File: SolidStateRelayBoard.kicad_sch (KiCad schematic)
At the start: 36 parts, among them J1 CONTROL_BUS, J2 GND, J4 SolenoidValveOutput1_5, J5 SolenoidValveOutput6_10, T1 48VA Transformer 240VAC/24VAC, U1 AQH3223A, U10 AQH3223A, U2 AQH3223A, U3 AQH3223A, U4 AQH3223A, U5 AQH3223A, U6 AQH3223A, U7 AQH3223A, U8 AQH3223A, U9 AQH3223A

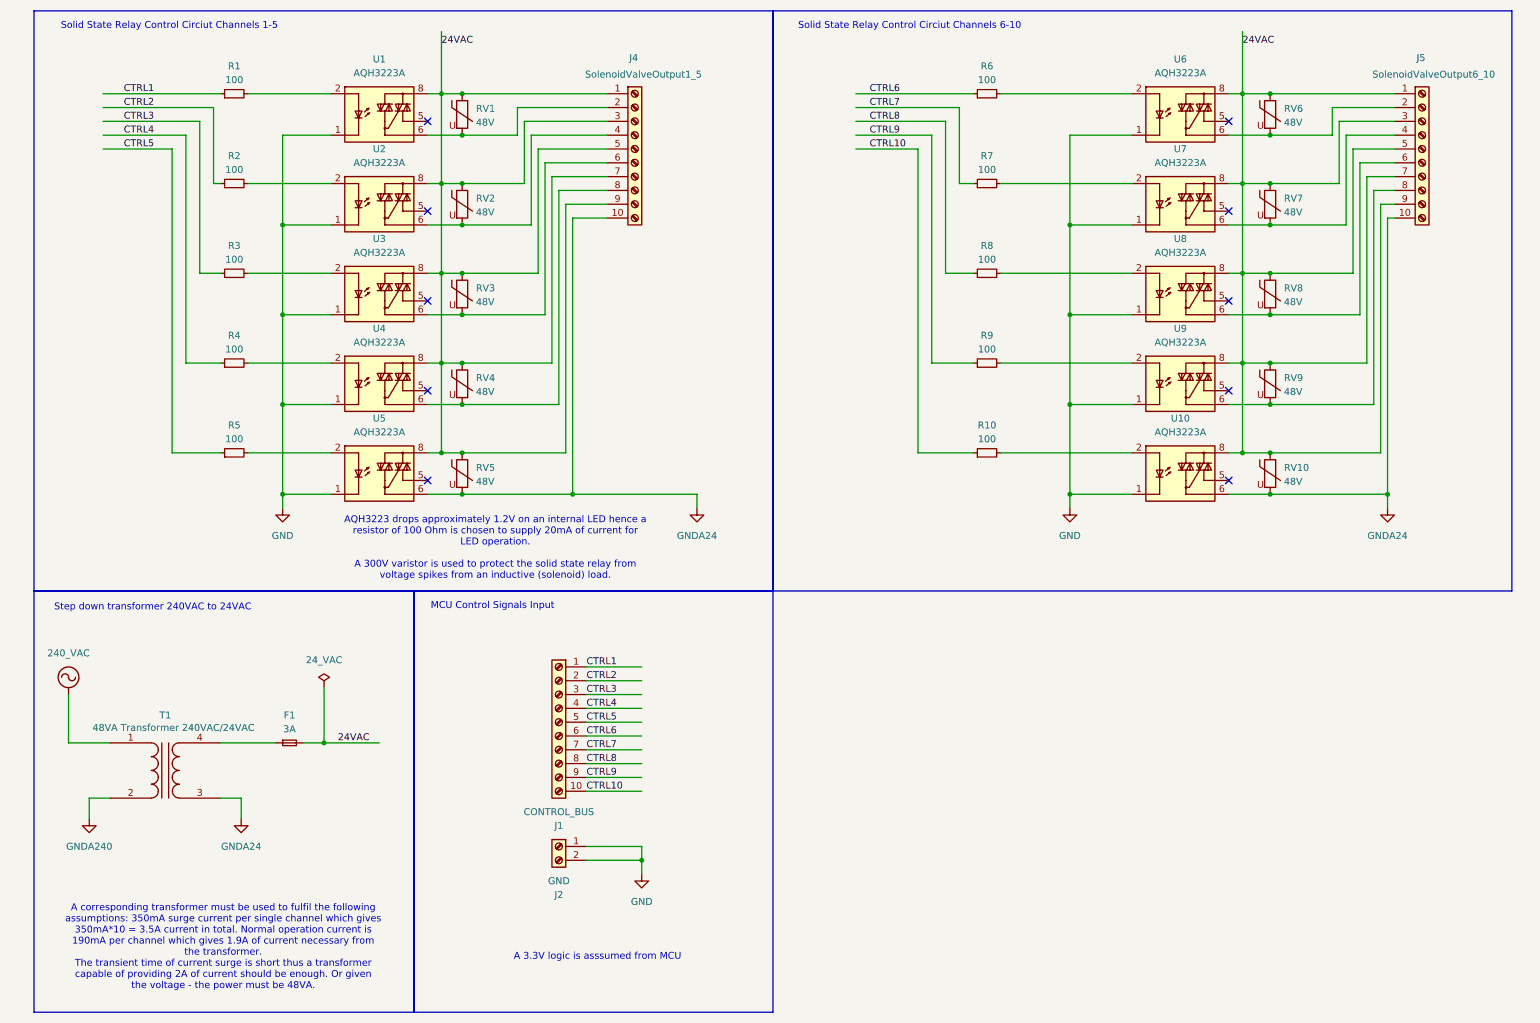
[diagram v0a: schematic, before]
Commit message: Add layout and 3D model
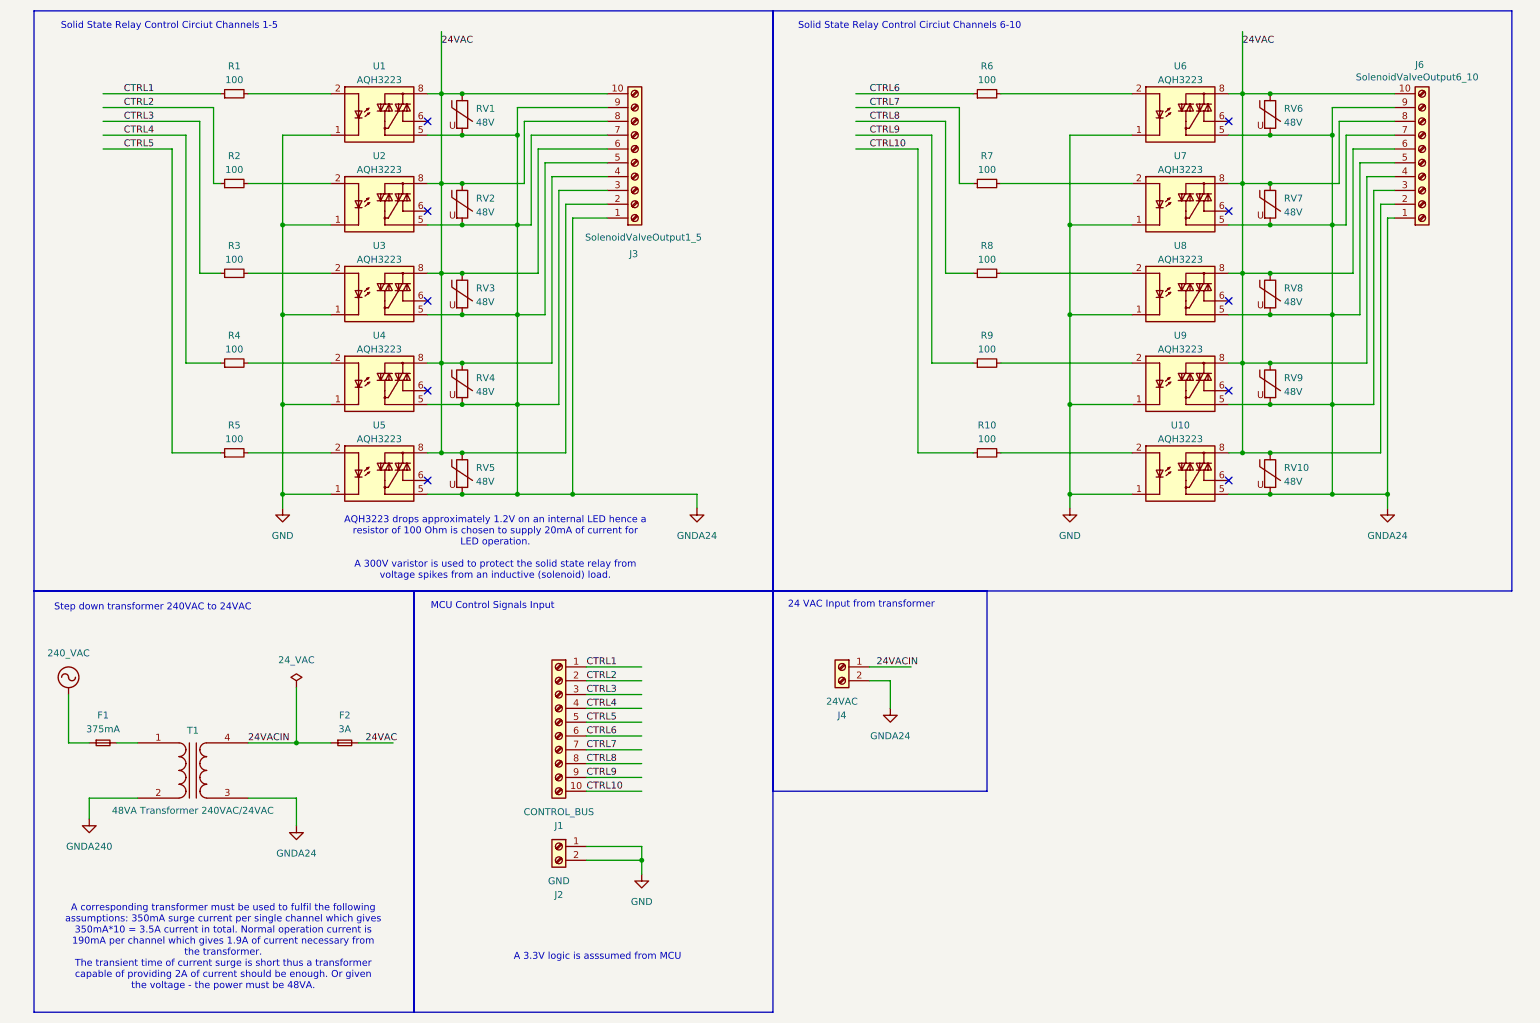
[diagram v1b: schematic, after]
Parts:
- removed J4: SolenoidValveOutput1_5, symbol Connector:Screw_Terminal_01x10
- removed J5: SolenoidValveOutput6_10, symbol Connector:Screw_Terminal_01x10
- removed U1, U10, U2, U3, U4, U5, U6, U7, U8, U9: AQH3223A, Package_SO:SSO-7-8_6.4x9.78mm_P2.54mm, symbol Relay_SolidState:AQH3223A
- added F2: 3A, Fuse:Fuseholder_Cylinder-5x20mm_Schurter_0031_8201_Horizontal_Open, symbol Device:Fuse_Small
- added J3: SolenoidValveOutput1_5, TerminalBlock_4Ucon:TerminalBlock_4Ucon_1x10_P3.50mm_Horizontal, symbol Connector:Screw_Terminal_01x10
- added J4: 24VAC, TerminalBlock_4Ucon:TerminalBlock_4Ucon_1x02_P3.50mm_Horizontal, symbol Connector:Screw_Terminal_01x02
- added J6: SolenoidValveOutput6_10, TerminalBlock_4Ucon:TerminalBlock_4Ucon_1x10_P3.50mm_Horizontal, symbol Connector:Screw_Terminal_01x10
- added U1, U10, U2, U3, U4, U5, U6, U7, U8, U9: AQH3223, Package_DIP:DIP-8-N7_W7.62mm, symbol Relay_SolidState:AQH3223
- F1: value 3A -> 375mA; footprint (none) -> Fuse:Fuseholder_Clip-5x20mm_Eaton_1A5601-01_Inline_P20.80x6.76mm_D1.70mm_Horizontal
- J1: footprint (none) -> TerminalBlock:TerminalBlock_Xinya_XY308-2.54-10P_1x10_P2.54mm_Horizontal
- J2: footprint (none) -> TerminalBlock:TerminalBlock_Xinya_XY308-2.54-2P_1x02_P2.54mm_Horizontal
- R1, R10, R2, R3, R4, R5, R6, R7, R8, R9: footprint (none) -> Resistor_SMD:R_0805_2012Metric
- RV1, RV10, RV2, RV3, RV4, RV5, RV6, RV7, RV8, RV9: footprint (none) -> Varistor:RV_Disc_D12mm_W3.9mm_P7.5mm
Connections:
- net 240_VAC: now also F1.1; no longer T1.1 (AA)
- net 24VAC: now also F2.2, J3.10 (Pin_10), J3.2 (Pin_2), J3.4 (Pin_4), J3.6 (Pin_6), J3.8 (Pin_8), J6.10 (Pin_10), J6.2 (Pin_2), J6.4 (Pin_4), J6.6 (Pin_6), J6.8 (Pin_8), U1.8, U10.8, U2.8, U3.8, U4.8, U5.8, U6.8, U7.8, U8.8, U9.8; no longer F1.2
- net GND: now also U1.1, U1.3, U1.4, U10.1, U10.3, U10.4, U2.1, U2.3, U2.4, U3.1, U3.3, U3.4, U4.1, U4.3, U4.4, U5.1, U5.3, U5.4, U6.1, U6.3, U6.4, U7.1, U7.3, U7.4, U8.1, U8.3, U8.4, U9.1, U9.3, U9.4
- net GNDA24: now also RV1.2, RV2.2, RV3.2, RV4.2, RV6.2, RV7.2, RV8.2, RV9.2, J3.1 (Pin_1), J3.3 (Pin_3), J3.5 (Pin_5), J3.7 (Pin_7), J3.9 (Pin_9), J4.2 (Pin_2), J6.1 (Pin_1), J6.3 (Pin_3), J6.5 (Pin_5), J6.7 (Pin_7), J6.9 (Pin_9), U1.5, U10.5, U2.5, U3.5, U4.5, U5.5, U6.5, U7.5, U8.5, U9.5
- net at R2.2: now also U2.2
- net at R9.2: now also U9.2
- net at R6.2: now also U6.2
- net at R3.2: now also U3.2
- net at R8.2: now also U8.2
- net at R1.2: now also U1.2
- net at R4.2: now also U4.2
- net at R5.2: now also U5.2
- net at R7.2: now also U7.2
- net at R10.2: now also U10.2
- net 24VACIN: now reaches T1.4 (SB)
- net 24VACIN: now also F2.1, J4.1 (Pin_1); no longer F1.1
- new net: F1.2, T1.1 (AA)
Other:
- note added: "24 VAC Input from transformer"
- moved on the sheet: T1
